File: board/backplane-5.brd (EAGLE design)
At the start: 100 x 100 mm, 146 parts, among them CN1 RJ45JACK90, CN2 4PINCONNFEMALE-1.6, CN3 4PINCONNFEMALE-1.6, CN4 4PINCONNFEMALE-1.6, CN5 4PINCONNFEMALE-1.6, CN6 4PINCONNFEMALE-1.6, U1 AMS1117-5.0, U10 RT9193, U11 KSZ9897, U12 KSZ8081MLX, U13 STM32F217-100, U2 AMS1117-5.0, U3 AMS1117-5.0, U4 AMS1117-5.0, U5 AMS1117-5.0, U6 AMS1117-2.5, U7 AMS1117-1.2, U8 RT9193, U9 AMS1117-5.0, Y1 25MHz, Y2 25MHz, Y3 25MHz

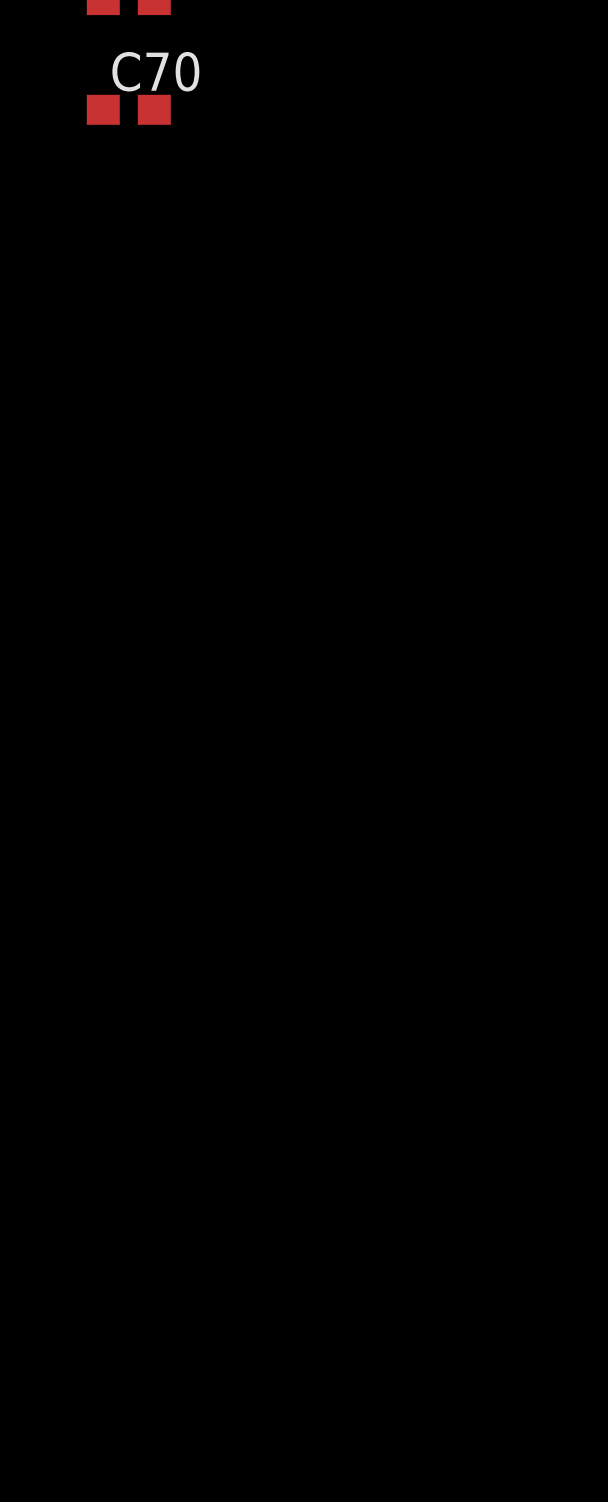
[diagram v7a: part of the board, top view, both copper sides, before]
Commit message: Added power to the STM32 and its decoupling caps
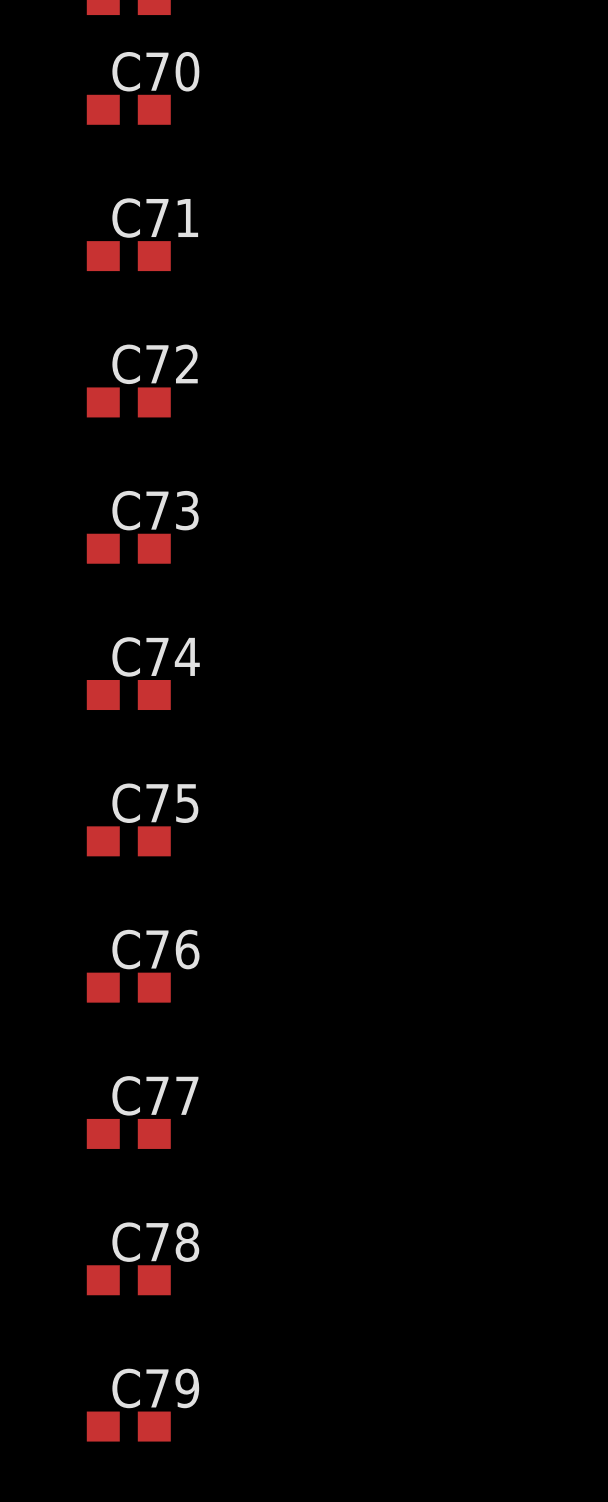
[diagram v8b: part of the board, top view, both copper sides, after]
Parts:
- added C71: 100nF, tuetuopay:0603
- added C72, C73, C74, C75, C76, C77, C78, C79: 10nF, tuetuopay:0603
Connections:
- new net N$23: C71.1, U13.14
- net 3V3-STM32: now also C72.1, C73.1, C74.1, C75.1, C76.1, C77.1, C78.1, C79.1, U13.100, U13.11, U13.19, U13.21, U13.22, U13.28, U13.50, U13.75
- net GND: now also C71.2, C72.2, C73.2, C74.2, C75.2, C76.2, C77.2, C78.2, C79.2, U13.10, U13.20, U13.27, U13.74
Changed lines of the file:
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@@
 <element name="C69" library="tuetuopay" package="0603" value="8pF" x="-151.1808" y="-538.0736"/>
 <element name="C70" library="tuetuopay" package="0603" value="8pF" x="-151.1808" y="-541.7312"/>
+<element name="C71" library="tuetuopay" package="0603" value="100nF" x="-151.1808" y="-546.608"/>
+<element name="C72" library="tuetuopay" package="0603" value="10nF" x="-151.1808" y="-551.4848"/>
+<element name="C73" library="tuetuopay" package="0603" value="10nF" x="-151.1808" y="-556.3616"/>
+<element name="C74" library="tuetuopay" package="0603" value="10nF" x="-151.1808" y="-561.2384"/>
+<element name="C75" library="tuetuopay" package="0603" value="10nF" x="-151.1808" y="-566.1152"/>
+<element name="C76" library="tuetuopay" package="0603" value="10nF" x="-151.1808" y="-570.992"/>
+<element name="C77" library="tuetuopay" package="0603" value="10nF" x="-151.1808" y="-575.8688"/>
+<element name="C78" library="tuetuopay" package="0603" value="10nF" x="-151.1808" y="-580.7456"/>
+<element name="C79" library="tuetuopay" package="0603" value="10nF" x="-151.1808" y="-585.6224"/>
 </elements>
 <signals>
@@
 <contactref element="C70" pad="2"/>
 <contactref element="C69" pad="2"/>
+<contactref element="C71" pad="2"/>
+<contactref element="U13" pad="10"/>
+<contactref element="U13" pad="20"/>
+<contactref element="U13" pad="27"/>
+<contactref element="U13" pad="74"/>
+<contactref element="C72" pad="2"/>
+<contactref element="C79" pad="2"/>
+<contactref element="C73" pad="2"/>
+<contactref element="C74" pad="2"/>
+<contactref element="C75" pad="2"/>
+<contactref element="C76" pad="2"/>
+<contactref element="C77" pad="2"/>
+<contactref element="C78" pad="2"/>
 <wire x1="-106.26" y1="-387.35" x2="-106.26" y2="-400.05" width="0" layer="19" extent="1-1"/>
 <wire x1="-106.26" y1="-374.65" x2="-106.26" y2="-387.35" width="0" layer="19" extent="1-1"/>
@@
 <wire x1="-145.2" y1="-483.87" x2="-145.2" y2="-478.79" width="0" layer="19" extent="1-1"/>
 <wire x1="-134.62" y1="-509.27" x2="-145.2" y2="-483.87" width="0" layer="19" extent="1-1"/>
-<wire x1="-150.3308" y1="-538.0736" x2="-134.62" y2="-509.27" width="0" layer="19" extent="1-1"/>
+<wire x1="-143.8792" y1="-518.538" x2="-134.62" y2="-509.27" width="0" layer="19" extent="1-1"/>
+<wire x1="-139.8792" y1="-534.038" x2="-143.8792" y2="-518.538" width="0" layer="19" extent="1-1"/>
+<wire x1="-134.8792" y1="-534.038" x2="-139.8792" y2="-534.038" width="0" layer="19" extent="1-1"/>
+<wire x1="-130.6292" y1="-531.788" x2="-134.8792" y2="-534.038" width="0" layer="19" extent="1-1"/>
+<wire x1="-150.3308" y1="-538.0736" x2="-139.8792" y2="-534.038" width="0" layer="19" extent="1-1"/>
 <wire x1="-150.3308" y1="-541.7312" x2="-150.3308" y2="-538.0736" width="0" layer="19" extent="1-1"/>
+<wire x1="-150.3308" y1="-546.608" x2="-150.3308" y2="-541.7312" width="0" layer="19" extent="1-1"/>
+<wire x1="-150.3308" y1="-551.4848" x2="-150.3308" y2="-546.608" width="0" layer="19" extent="1-1"/>
+<wire x1="-150.3308" y1="-556.3616" x2="-150.3308" y2="-551.4848" width="0" layer="19" extent="1-1"/>
+<wire x1="-150.3308" y1="-561.2384" x2="-150.3308" y2="-556.3616" width="0" layer="19" extent="1-1"/>
+<wire x1="-150.3308" y1="-566.1152" x2="-150.3308" y2="-561.2384" width="0" layer="19" extent="1-1"/>
+<wire x1="-150.3308" y1="-570.992" x2="-150.3308" y2="-566.1152" width="0" layer="19" extent="1-1"/>
+<wire x1="-150.3308" y1="-575.8688" x2="-150.3308" y2="-570.992" width="0" layer="19" extent="1-1"/>
+<wire x1="-150.3308" y1="-580.7456" x2="-150.3308" y2="-575.8688" width="0" layer="19" extent="1-1"/>
+<wire x1="-150.3308" y1="-585.6224" x2="-150.3308" y2="-580.7456" width="0" layer="19" extent="1-1"/>
 <wire x1="-76.62" y1="-128.27" x2="-84.24" y2="-219.71" width="0" layer="19" extent="1-1"/>
 <wire x1="12.44" y1="5.83" x2="-76.62" y2="-128.27" width="0" layer="19" extent="1-1"/>
@@
 <wire x1="8.5344" y1="23.6084" x2="9.9292" y2="23.6084" width="0.4064" layer="1"/>
 <wire x1="9.9292" y1="23.6084" x2="10.0228" y2="23.702" width="0.4064" layer="1"/>
+<contactref element="U13" pad="11"/>
+<contactref element="U13" pad="19"/>
+<contactref element="U13" pad="21"/>
+<contactref element="U13" pad="22"/>
+<contactref element="U13" pad="28"/>
+<contactref element="U13" pad="50"/>
+<contactref element="U13" pad="75"/>
+<contactref element="U13" pad="100"/>
+<contactref element="C72" pad="1"/>
+<contactref element="C79" pad="1"/>
+<contactref element="C78" pad="1"/>
+<contactref element="C77" pad="1"/>
+<contactref element="C76" pad="1"/>
+<contactref element="C75" pad="1"/>
+<contactref element="C74" pad="1"/>
+<contactref element="C73" pad="1"/>
+<wire x1="-152.0308" y1="-580.7456" x2="-152.0308" y2="-585.6224" width="0" layer="19" extent="1-1"/>
+<wire x1="-152.0308" y1="-575.8688" x2="-152.0308" y2="-580.7456" width="0" layer="19" extent="1-1"/>
+<wire x1="-152.0308" y1="-570.992" x2="-152.0308" y2="-575.8688" width="0" layer="19" extent="1-1"/>
+<wire x1="-152.0308" y1="-566.1152" x2="-152.0308" y2="-570.992" width="0" layer="19" extent="1-1"/>
+<wire x1="-152.0308" y1="-561.2384" x2="-152.0308" y2="-566.1152" width="0" layer="19" extent="1-1"/>
+<wire x1="-152.0308" y1="-556.3616" x2="-152.0308" y2="-561.2384" width="0" layer="19" extent="1-1"/>
+<wire x1="-152.0308" y1="-551.4848" x2="-152.0308" y2="-556.3616" width="0" layer="19" extent="1-1"/>
+<wire x1="-146.1292" y1="-532.288" x2="-152.0308" y2="-551.4848" width="0" layer="19" extent="1-1"/>
+<wire x1="-139.3792" y1="-534.038" x2="-146.1292" y2="-532.288" width="0" layer="19" extent="1-1"/>
+<wire x1="-135.3792" y1="-534.038" x2="-139.3792" y2="-534.038" width="0" layer="19" extent="1-1"/>
+<wire x1="-134.3792" y1="-534.038" x2="-135.3792" y2="-534.038" width="0" layer="19" extent="1-1"/>
+<wire x1="-133.8792" y1="-534.038" x2="-134.3792" y2="-534.038" width="0" layer="19" extent="1-1"/>
+<wire x1="-130.6292" y1="-531.288" x2="-133.8792" y2="-534.038" width="0" layer="19" extent="1-1"/>
+<wire x1="-130.6292" y1="-520.288" x2="-130.6292" y2="-531.288" width="0" layer="19" extent="1-1"/>
+<wire x1="-144.3792" y1="-518.538" x2="-146.1292" y2="-532.288" width="0" layer="19" extent="1-1"/>
+<wire x1="8.5344" y1="23.6084" x2="-130.6292" y2="-520.288" width="0" layer="19" extent="1-1"/>
 </signal>
 <signal name="N$1">
@@
 <wire x1="-138.8792" y1="-534.038" x2="-148.9244" y2="-531.368" width="0" layer="19" extent="1-1"/>
 </signal>
+<signal name="N$23">
+<contactref element="C71" pad="1"/>
+<contactref element="U13" pad="14"/>
+<wire x1="-137.8792" y1="-534.038" x2="-152.0308" y2="-546.608" width="0" layer="19" extent="1-1"/>
+</signal>
 </signals>
